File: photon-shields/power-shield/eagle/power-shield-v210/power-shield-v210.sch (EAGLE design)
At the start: 60 parts, among them U1 BQ24030BQ24030, U2 MAX1704X, U3 REGULATORSRT8259GE

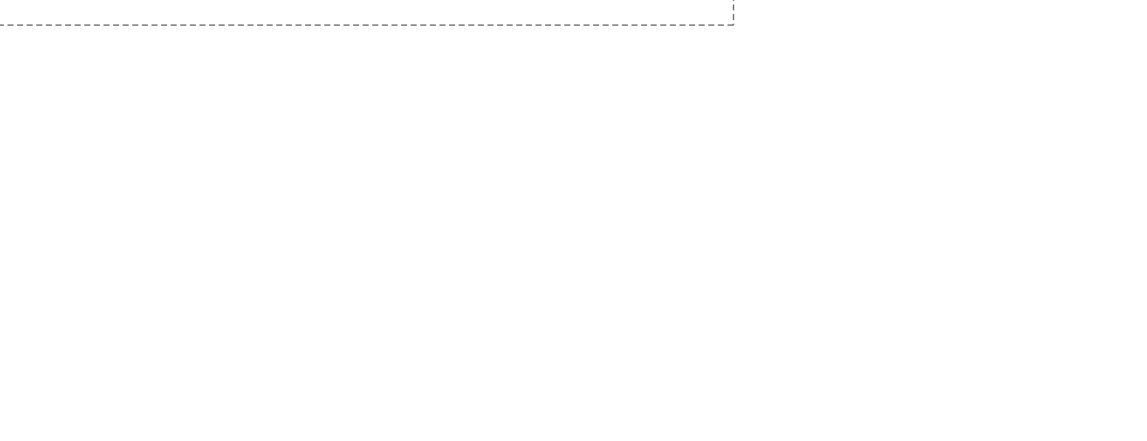
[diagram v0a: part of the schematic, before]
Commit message: added rev numbers to schematic sheets and regenerated the PDFs
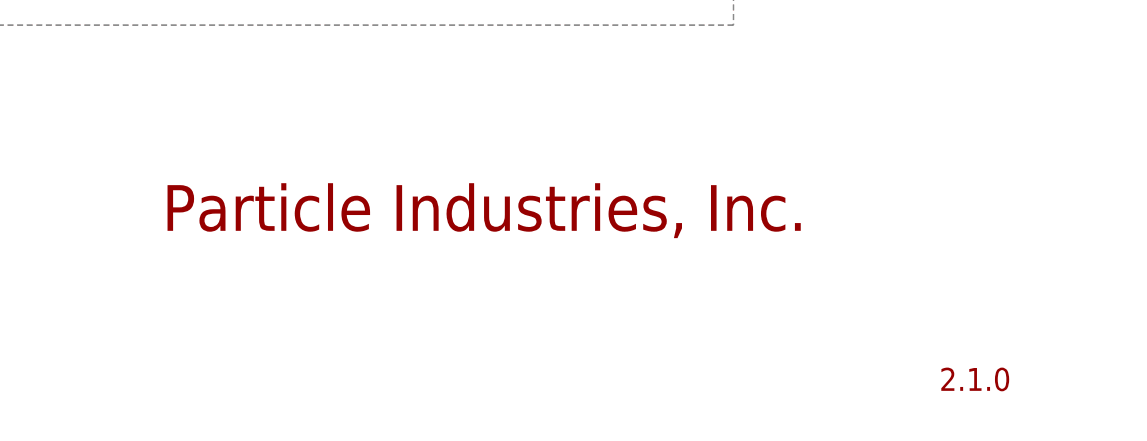
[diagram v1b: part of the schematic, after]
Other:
- note added: "2.1.0"
- note added: "Particle Industries, Inc."
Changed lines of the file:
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@@
 <setting verticaltext="up"/>
 </settings>
-<grid distance="0.1" unitdist="inch" unit="inch" style="lines" multiple="1" display="yes" altdistance="0.01" altunitdist="inch" altunit="inch"/>
+<grid distance="0.1" unitdist="inch" unit="inch" style="lines" multiple="1" display="no" altdistance="0.01" altunitdist="inch" altunit="inch"/>
 <layers>
 <layer number="1" name="Top" color="4" fill="1" visible="no" active="no"/>
@@
 with this information.
 Particle is a registered trademark.</text>
+<text x="375.92" y="7.62" size="2.54" layer="94">2.1.0</text>
+<text x="289.56" y="25.4" size="5.08" layer="94">Particle Industries, Inc.</text>
 </plain>
 <instances>
